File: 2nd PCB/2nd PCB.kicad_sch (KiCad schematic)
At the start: 11 parts

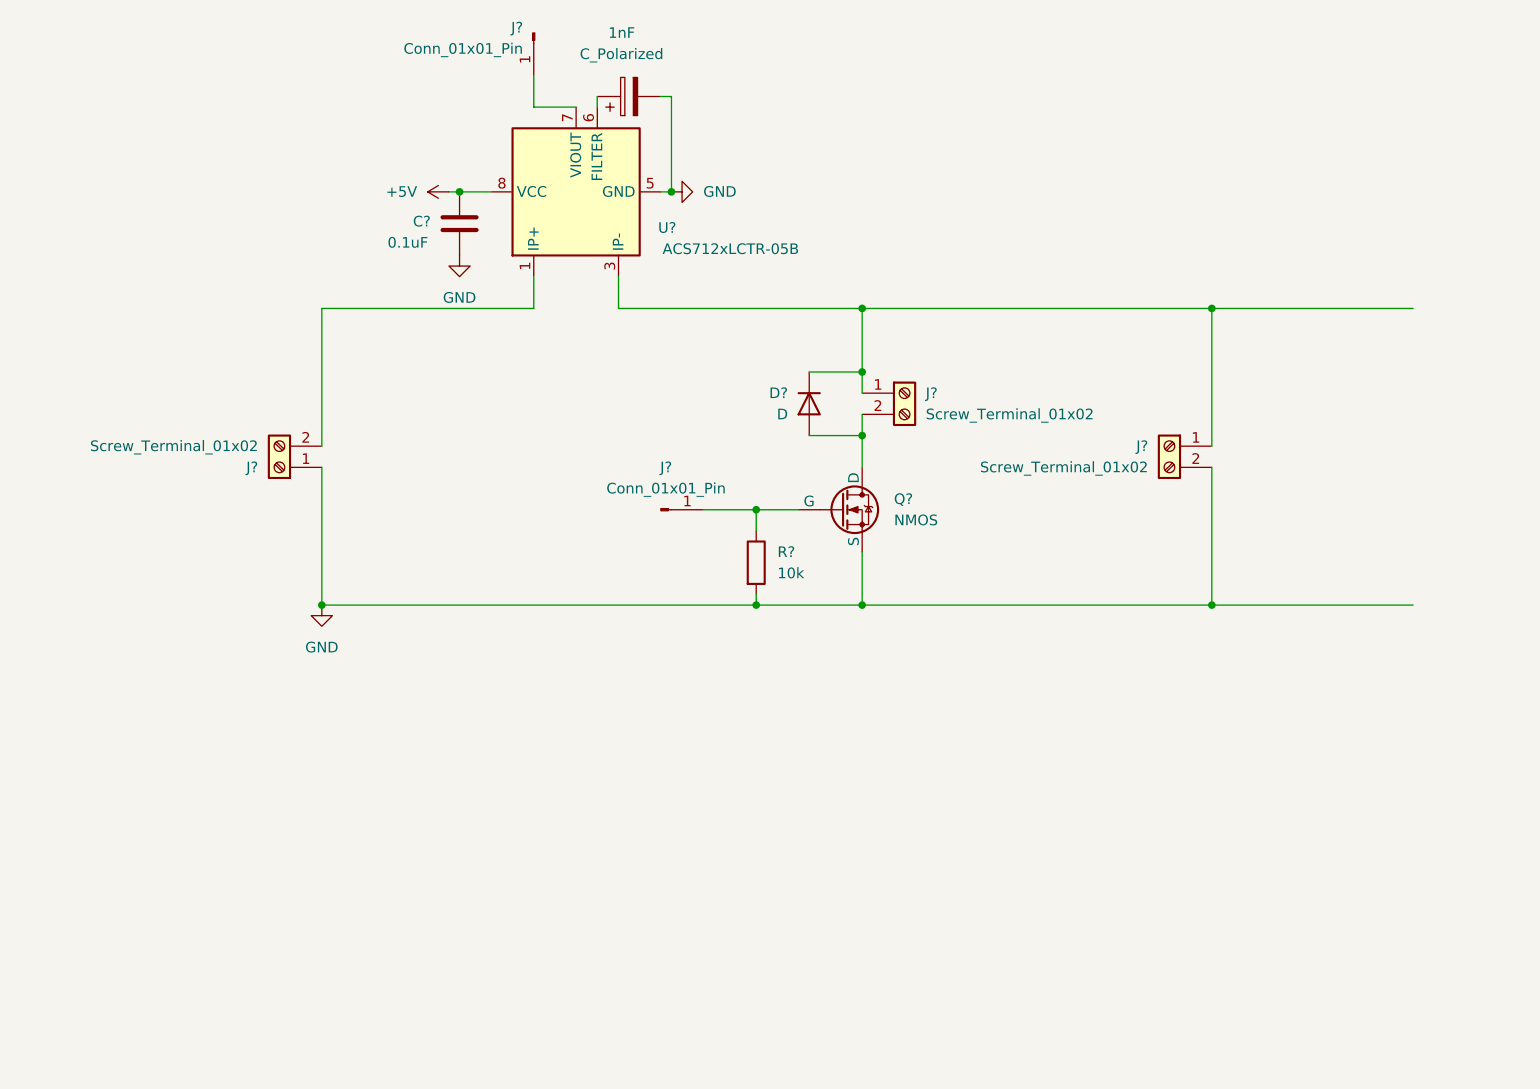
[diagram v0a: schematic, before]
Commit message: Added linear voltage regulator to 2nd PCB
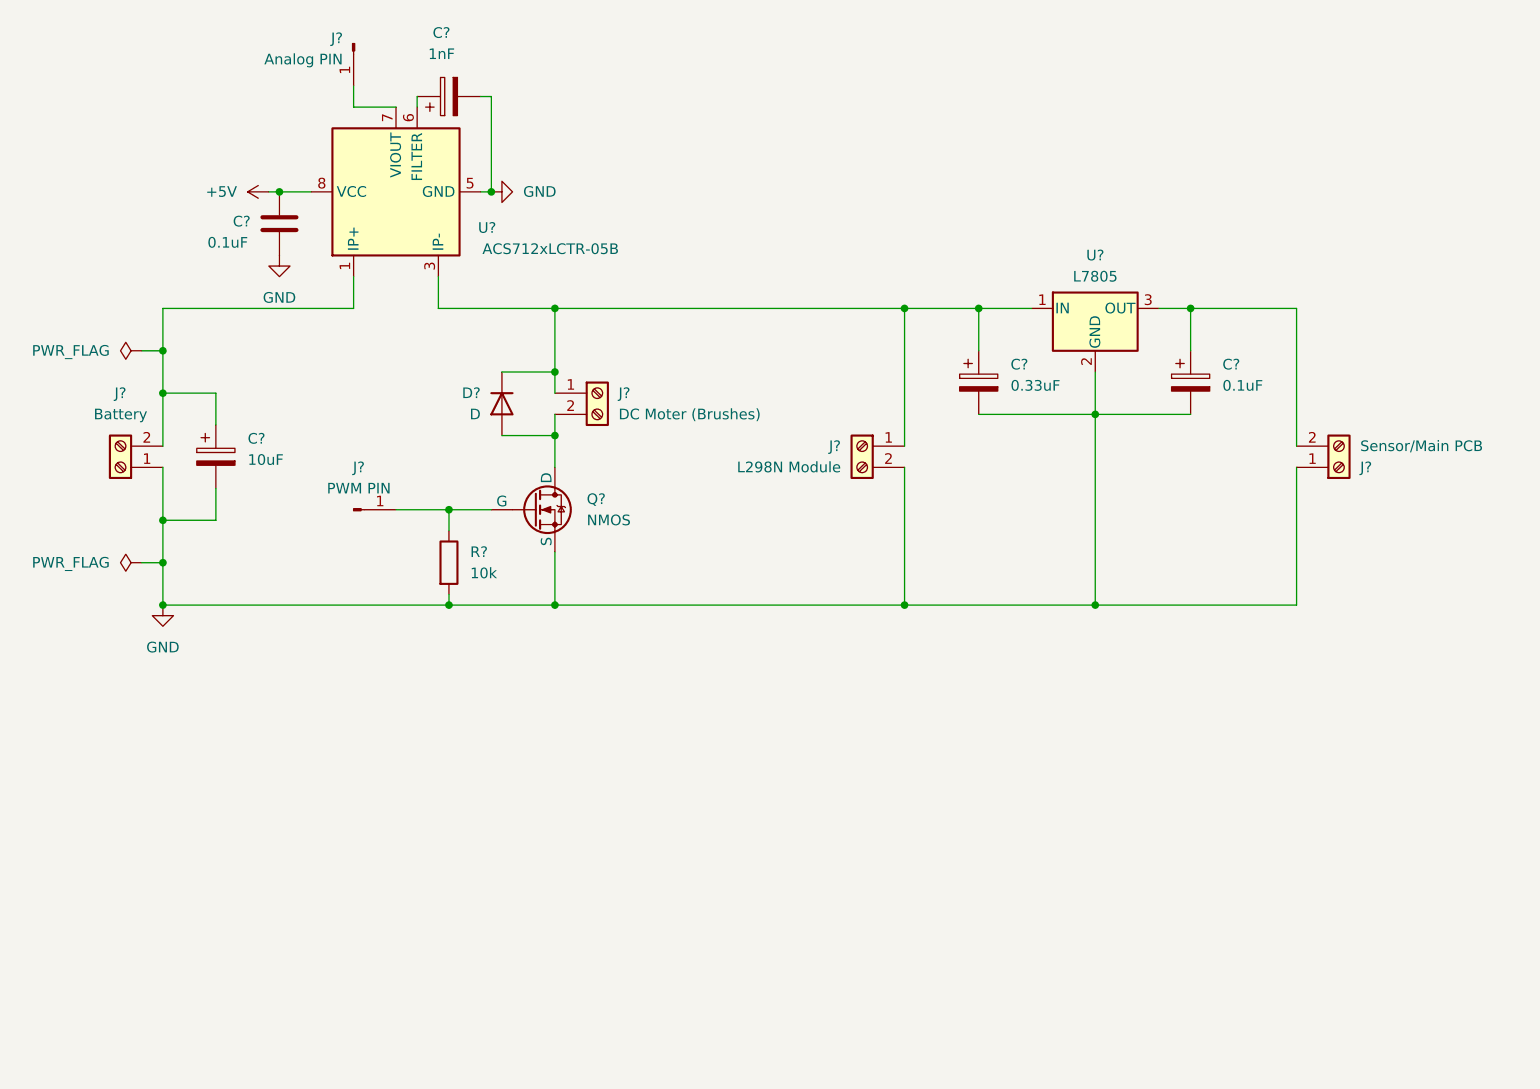
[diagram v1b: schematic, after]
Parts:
- added C?: 10uF, symbol Device:C_Polarized
- added C?: 0.1uF, symbol Device:C_Polarized
- added C?: 0.33uF, symbol Device:C_Polarized
- added J?: Sensor/Main PCB, symbol Connector:Screw_Terminal_01x02
- added U?: L7805, symbol Regulator_Linear:L7805
- C?: renamed from 1nF; value C_Polarized -> 1nF
- J?: value Conn_01x01_Pin -> Analog PIN
- J?: value Conn_01x01_Pin -> PWM PIN
- J?: value Screw_Terminal_01x02 -> Battery
- J?: value Screw_Terminal_01x02 -> DC Moter (Brushes)
- J?: value Screw_Terminal_01x02 -> L298N Module
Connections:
- net GND: now also C?.2, C?.2, C?.2, J?.1 (Pin_1), U?.2 (GND)
- net at J?.2 (Pin_2), U?.1 (IP+), U?.2 (IP+): now also C?.1
- net at D?.1 (K), J?.1 (Pin_1), J?.1 (Pin_1)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: now also C?.1, U?.1 (IN)
- new net: C?.1, J?.2 (Pin_2), U?.3 (OUT)
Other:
- moved on the sheet: C?, D?, J?, Q?, R?, U?

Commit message: First attempt at designing the board for the second PCB
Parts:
- removed C?: 1nF, symbol Device:C_Polarized
- removed C?: 0.1uF, symbol Device:C
- added C2: 0.1uF, Capacitor_THT:CP_Radial_D5.0mm_P2.50mm, symbol Device:C_Polarized
- added C3: 1nF, Capacitor_THT:C_Disc_D3.0mm_W2.0mm_P2.50mm, symbol Device:C
- C1, C4, C5: renamed from C?; footprint (none) -> Capacitor_THT:CP_Radial_D5.0mm_P2.50mm
- D1: renamed from D?; footprint (none) -> Diode_THT:D_DO-41_SOD81_P10.16mm_Horizontal
- J1, J4, J5, J6: renamed from J?; footprint (none) -> TerminalBlock:TerminalBlock_bornier-2_P5.08mm
- J2: renamed from J?; value Analog PIN -> ADC PIN; footprint (none) -> Connector_PinHeader_2.54mm:PinHeader_1x01_P2.54mm_Vertical
- J3: renamed from J?; footprint (none) -> Connector_PinHeader_2.54mm:PinHeader_1x01_P2.54mm_Vertical
- Q1: renamed from Q?; footprint (none) -> Package_TO_SOT_THT:TO-220-3_Vertical
- R1: renamed from R?; footprint (none) -> Resistor_THT:R_Axial_DIN0207_L6.3mm_D2.5mm_P10.16mm_Horizontal
- U2: renamed from U?; footprint (none) -> Package_TO_SOT_THT:TO-220-3_Vertical
- gave numbers to parts that had none: 1
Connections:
- net +5V: now also C5.1, J6.2 (Pin_2), U2.3 (OUT), C2.1
- net GND: now also C2.2, C3.1
- net at U1.6 (FILTER): now also C3.2

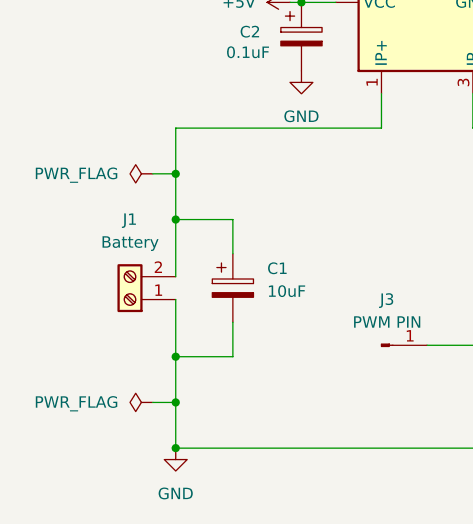
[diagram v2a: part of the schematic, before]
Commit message: Added to main PCB board
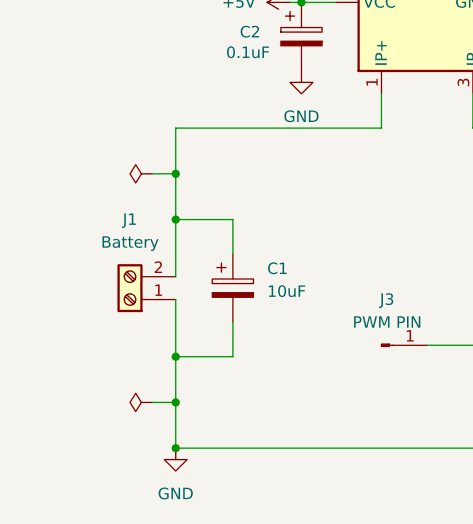
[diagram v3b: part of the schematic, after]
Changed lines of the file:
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@@
 				)
 				(justify left)
+				(hide yes)
 			)
 		)
@@
 				)
 				(justify left)
-			)
-		)
+				(hide yes)
+			)
+		)

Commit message: finished the PCB board designs
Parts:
- added H1, H2, H3, H4: MountingHole, MountingHole:MountingHole_3.2mm_M3, symbol Mechanical:MountingHole

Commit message: First iteration of both PCB's send for review
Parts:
- D1: value D -> 1N4001
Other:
- note added: "+14V"
- note added: "GND"
- title: (none) -> 2nd PCB
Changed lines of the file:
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@@
 	(generator_version "8.0")
 	(paper "A4")
+	(title_block
+		(title "2nd PCB")
+		(date "2024-11-27")
+		(rev "1")
+	)
 	(junction
 		(at 60.96 80.01)
@@
 		)
 	)
+	(text "GND"
+		(exclude_from_sim no)
+		(at 51.562 89.154 0)
+		(effects
+			(font
+				(size 1.27 1.27)
+			)
+		)
+	)
+	(text "+14V"
+		(exclude_from_sim no)
+		(at 51.054 86.36 0)
+		(effects
+			(font
+				(size 1.27 1.27)
+			)
+		)
+	)
 	(netclass_flag ""
 		(length 1)
@@
 			(justify right bottom)
 		)
-		(property "Netclass" "Battery Power"
+		(property "Netclass" "14V Battery Power"
 			(at 108.95 86.9315 90)
 			(effects
@@
 			(justify left bottom)
 		)
-		(property "Netclass" "Battery Power"
+		(property "Netclass" "14V Battery Power"
 			(at 103.5685 68.85 0)
+			(effects
+				(font
+					(size 1.27 1.27)
+					(italic yes)
+				)
+				(justify left)
+				(hide yes)
+			)
+		)
+	)
+	(netclass_flag ""
+		(length 1)
+		(shape dot)
+		(at 100.33 46.99 270)
+		(fields_autoplaced yes)
+		(effects
+			(font
+				(size 1.27 1.27)
+			)
+			(justify right bottom)
+		)
+		(property "Netclass" "5V Power"
+			(at 101.33 46.2915 90)
 			(effects
 				(font
@@
 			(justify left bottom)
 		)
-		(property "Netclass" "Battery Power"
+		(property "Netclass" "14V Battery Power"
 			(at 65.4685 68.85 0)
-			(effects
-				(font
-					(size 1.27 1.27)
-					(italic yes)
-				)
-				(justify left)
-				(hide yes)
-			)
-		)
-	)
-	(netclass_flag ""
-		(length 1)
-		(shape dot)
-		(at 100.33 48.26 90)
-		(fields_autoplaced yes)
-		(effects
-			(font
-				(size 1.27 1.27)
-			)
-			(justify left bottom)
-		)
-		(property "Netclass" "5V Power"
-			(at 99.33 47.5615 90)
 			(effects
 				(font
@@
 			)
 		)
-		(property "Datasheet" "~"
+		(property "Datasheet" "https://docs.rs-online.com/0623/0900766b8157c7d5.pdf"
 			(at 55.88 88.9 0)
 			(effects
@@
 			)
 		)
-		(property "Datasheet" "https://ngspice.sourceforge.io/docs/ngspice-html-manual/manual.xhtml#cha_MOSFETs"
+		(property "Datasheet" "https://docs.rs-online.com/32cc/0900766b814c8cbb.pdf"
 			(at 105.41 106.68 0)
 			(effects
@@
 			)
 		)
-		(property "Datasheet" "~"
+		(property "Datasheet" "https://dk.rs-online.com/web/p/dc-motorer-jaevnstromsmotorer/2389737?gb=s"
 			(at 113.03 80.01 0)
 			(effects
@@
 			)
 		)
-		(property "Datasheet" "~"
+		(property "Datasheet" "https://docs.rs-online.com/0623/0900766b8157c7d5.pdf"
 			(at 201.93 88.9 0)
 			(effects
@@
 			)
 		)
-		(property "Datasheet" "~"
+		(property "Datasheet" "https://docs.rs-online.com/0623/0900766b8157c7d5.pdf"
 			(at 144.78 86.36 0)
 			(effects
@@
 			)
 		)
-		(property "Value" "D"
+		(property "Value" "1N4001"
 			(at 99.06 82.5499 90)
 			(effects
@@
 			)
 		)
-		(property "Datasheet" "~"
+		(property "Datasheet" "https://www.vishay.com/docs/88503/1n4001.pdf"
 			(at 101.6 81.28 0)
 			(effects

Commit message: Second revision
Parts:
- added C?: 100nF, symbol Device:C
- added R?: 10k, symbol Device:R
- added SW? (x2): SW_Push_Dual, symbol Switch:SW_Push_Dual
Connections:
- net +5V: now also C?.1, SW?.1
- net GND: now also C?.2, R?.2, SW?.1
- new net: R?.1, SW?.3
- new net INT0: SW?.4
- new net RESET: SW?.4
- no-connect marks 0 -> 3
